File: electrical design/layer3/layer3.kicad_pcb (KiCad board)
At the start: 2 copper layers, 150 x 137.9 mm, 42 parts, among them J1 SH1.0 5P, J10 SH1.0 2P, J11 LAYER1, J12 XH2.54 2P, J2 SH1.0 5P, J3 SH1.0 5P, J4 SH1.0 5P, J5 XH2.54 5P, J6 CAMERA1, J7 CAMERA2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

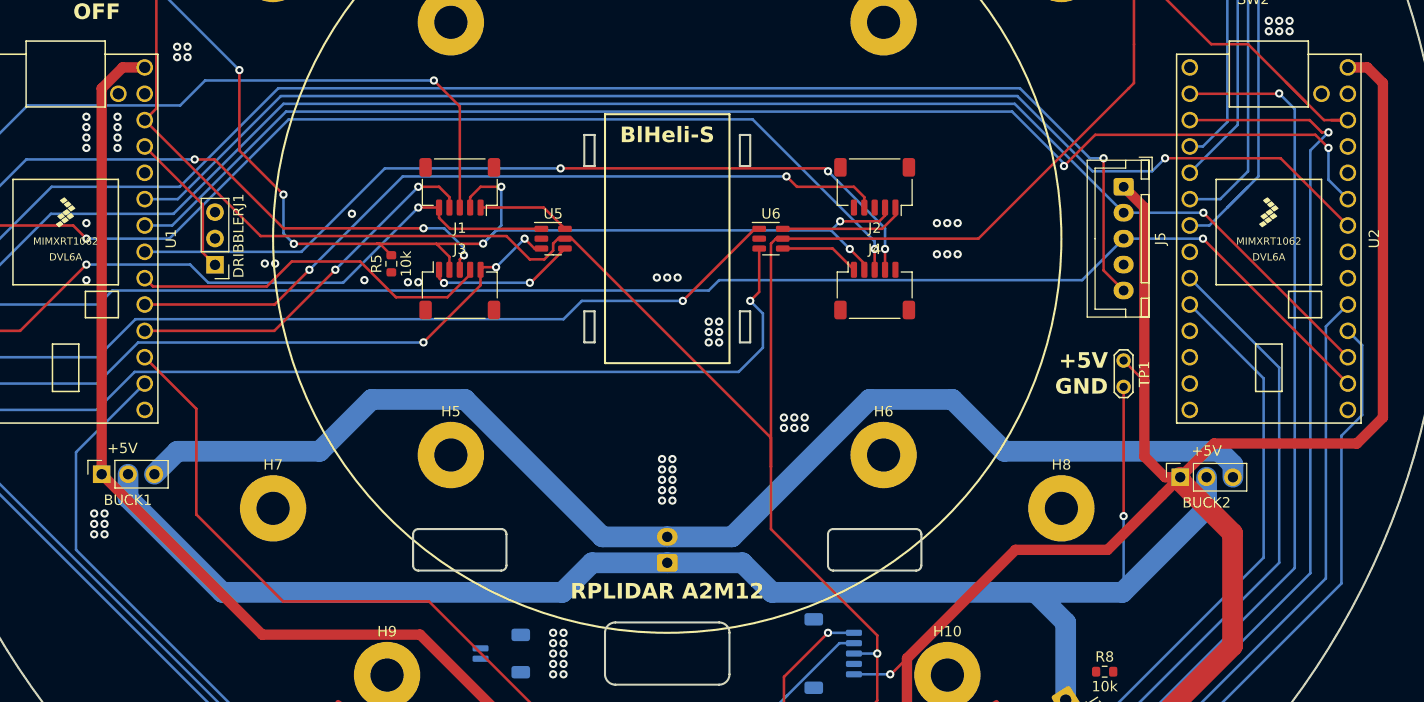
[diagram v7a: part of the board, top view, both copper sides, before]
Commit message: amend buck conv pinouts on l1 and l3
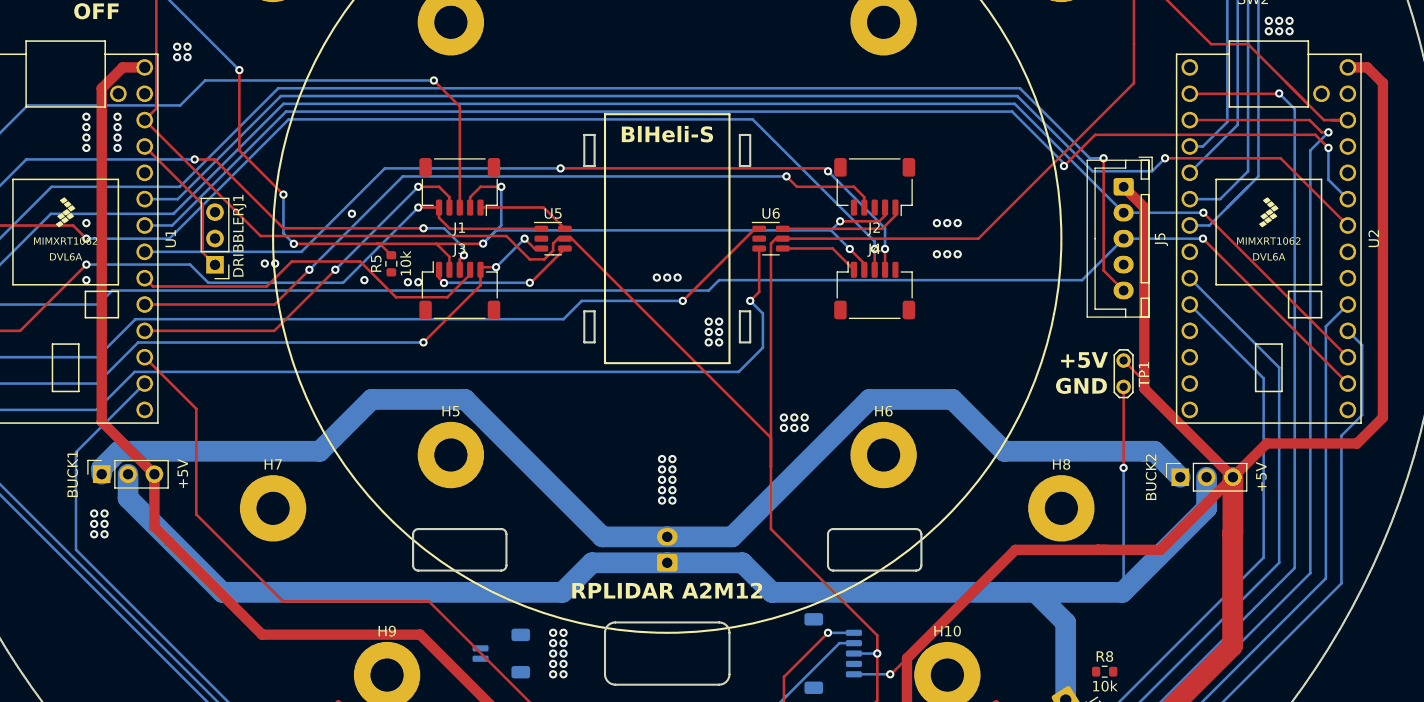
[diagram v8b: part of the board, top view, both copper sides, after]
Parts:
- BUCK1, BUCK2: footprint Connector_PinSocket_2.54mm:PinSocket_1x03_P2.54mm_Vertical -> Connector_PinSocket_2.54mm:TPS5430 Board
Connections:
- BUCK1 pad 1: +5V -> +12V
- BUCK1 pad 3: +12V -> +5V
- BUCK2 pad 1: +5V -> +12V
- BUCK2 pad 3: +12V -> +5V
- J12 pad 2: Net-(J12-Pin_2) -> +5V
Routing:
- net +5V: track 370.3 -> 363.7 mm
